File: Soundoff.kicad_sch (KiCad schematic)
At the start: 22 parts, among them J1 Debug, J2 USB-C Receptacle, J4 USB_A, SW1 Pushbutton 4.2x3.2mm 250gf, SW2 Pushbutton 4.2x3.2mm 250gf, U1 3.3V LDO, U16 TLP3123, U4 STM32F042G6Ux

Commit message: v2: make usb-c and pass data through
Signed-off-by: Sean Cross <sean@xobs.io>
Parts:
- removed J4: USB_A, Connector_USB:USB_A_Connfly_DS1095, symbol Connector:USB_A
- removed SW1, SW2: Pushbutton 4.2x3.2mm 250gf, Button_Switch_SMD:SW_Push_1P1T_XKB_TS-1187A, symbol Soundoff:Pushbutton Basic
- added C14, C15, C6: 4.7uF, Capacitor_SMD:C_0402_1005Metric, symbol Soundoff:C 4.7uF 10V 0402
- added C4, C5: 30pF, Capacitor_SMD:C_0603_1608Metric, symbol Device:C_Small
- added P1: Switched USB-C, Soundoff:USB-C-SMD_TYPE-C-31-G-07-1, symbol Soundoff:USB_C_Plug_P24
- added R9: R 5.1k 0402, Resistor_SMD:R_0402_1005Metric, symbol Soundoff:R 5.1k 0402
- added U2: CH334F, Package_DFN_QFN:QFN-24-1EP_4x4mm_P0.5mm_EP2.7x2.7mm, symbol Interface_USB:CH334F
- added U3: EMS4000RSW, Soundoff:QFN-10_1.4x1.8_Pitch0.4mm, symbol Soundoff:EMS4000RSW USB Mux
- added Y1: 12 MHz, 20pF, Crystal:Crystal_SMD_3225-4Pin_3.2x2.5mm, symbol Device:Crystal_GND24_Small
- J1: footprint Connector_PinHeader_2.54mm:PinHeader_1x05_P2.54mm_Vertical -> Connector_PinHeader_2.54mm:PinHeader_1x06_P2.54mm_Vertical; symbol Connector_Generic:Conn_01x05 -> Connector_Generic:Conn_01x06
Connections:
- net BOOT0: now also J1.6 (Pin_6)
- net DBG_USB_D+: now also U2.6 (DP4+); no longer J2.A6 (D+), J2.B6 (D+)
- net DBG_USB_D-: now also U2.5 (DM4-); no longer J2.A7 (D-), J2.B7 (D-)
- net GND: now also C14.2, C15.2, C4.2, C5.2, C6.2, P1.A1 (GND), P1.A12 (GND), P1.B1 (GND), P1.B12 (GND), P1.SH (SHIELD), R9.2, U2.18 (PSELF), U2.25 (GND), U3.3 (GND), U3.8 (EN), Y1.2 (G), Y1.4 (G)
- net VUSB: now also C6.1, U2.19 (V5)
- net 3.0V renamed 3.3V
- net 3.3V: now also C14.1, C15.1, U2.20 (VDD33_{LDO}), U3.9 (VDD)
- net 5V_CONTROL renamed PORT_EN
- net PORT_EN: now also U3.10 (SEL)
- net SWITCHED_5V renamed VUSB_SW
- net VUSB_SW: now also P1.A4 (VBUS), P1.A9 (VBUS), P1.B4 (VBUS), P1.B9 (VBUS)
- new net: P1.A5 (CC), R9.1
- new net: C4.1, U2.4 (XI), Y1.1
- new net: C5.1, U2.3 (XO), Y1.3
- new net TGT_SW_USB_D+: P1.A6 (D+), P1.B6 (D+), U3.7 (L1+)
- new net TGT_SW_USB_D-: P1.A7 (D-), P1.B7 (D-), U3.6 (L1-)
- new net TGT_USB_D+: U2.8 (DP3+), U3.1 (CO+)
- new net TGT_USB_D-: U2.7 (DM3-), U3.2 (CO-)
- new net UFP_USB_D+: J2.A6 (D+), J2.B6 (D+), U2.15 (DPU+)
- new net UFP_USB_D-: J2.A7 (D-), J2.B7 (D-), U2.14 (DMU-)
- no-connect marks 20 -> 42
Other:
- note added: "Switched Port"
- note removed: "Switched Power"
- moved on the sheet: C12, C13

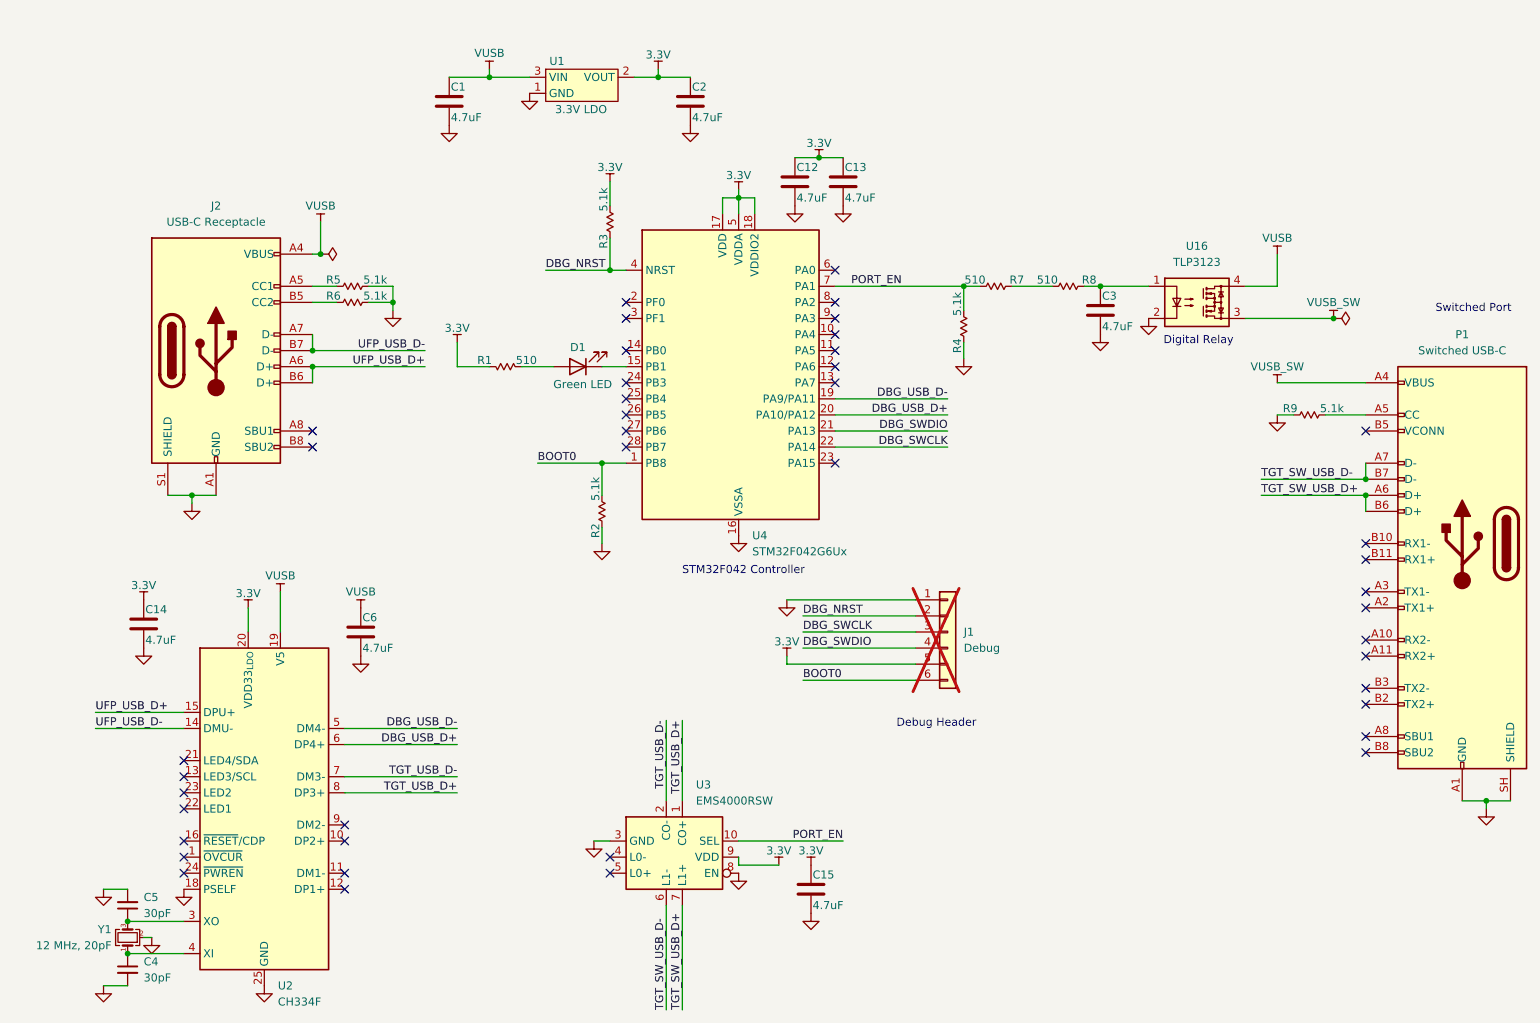
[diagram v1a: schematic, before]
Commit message: v3: fix usb polarity
The USB polarity was incorrect -- the DFP and UFP roles were swapped.
Change the connectors around to make it correct now.

Signed-off-by: Sean Cross <sean@xobs.io>
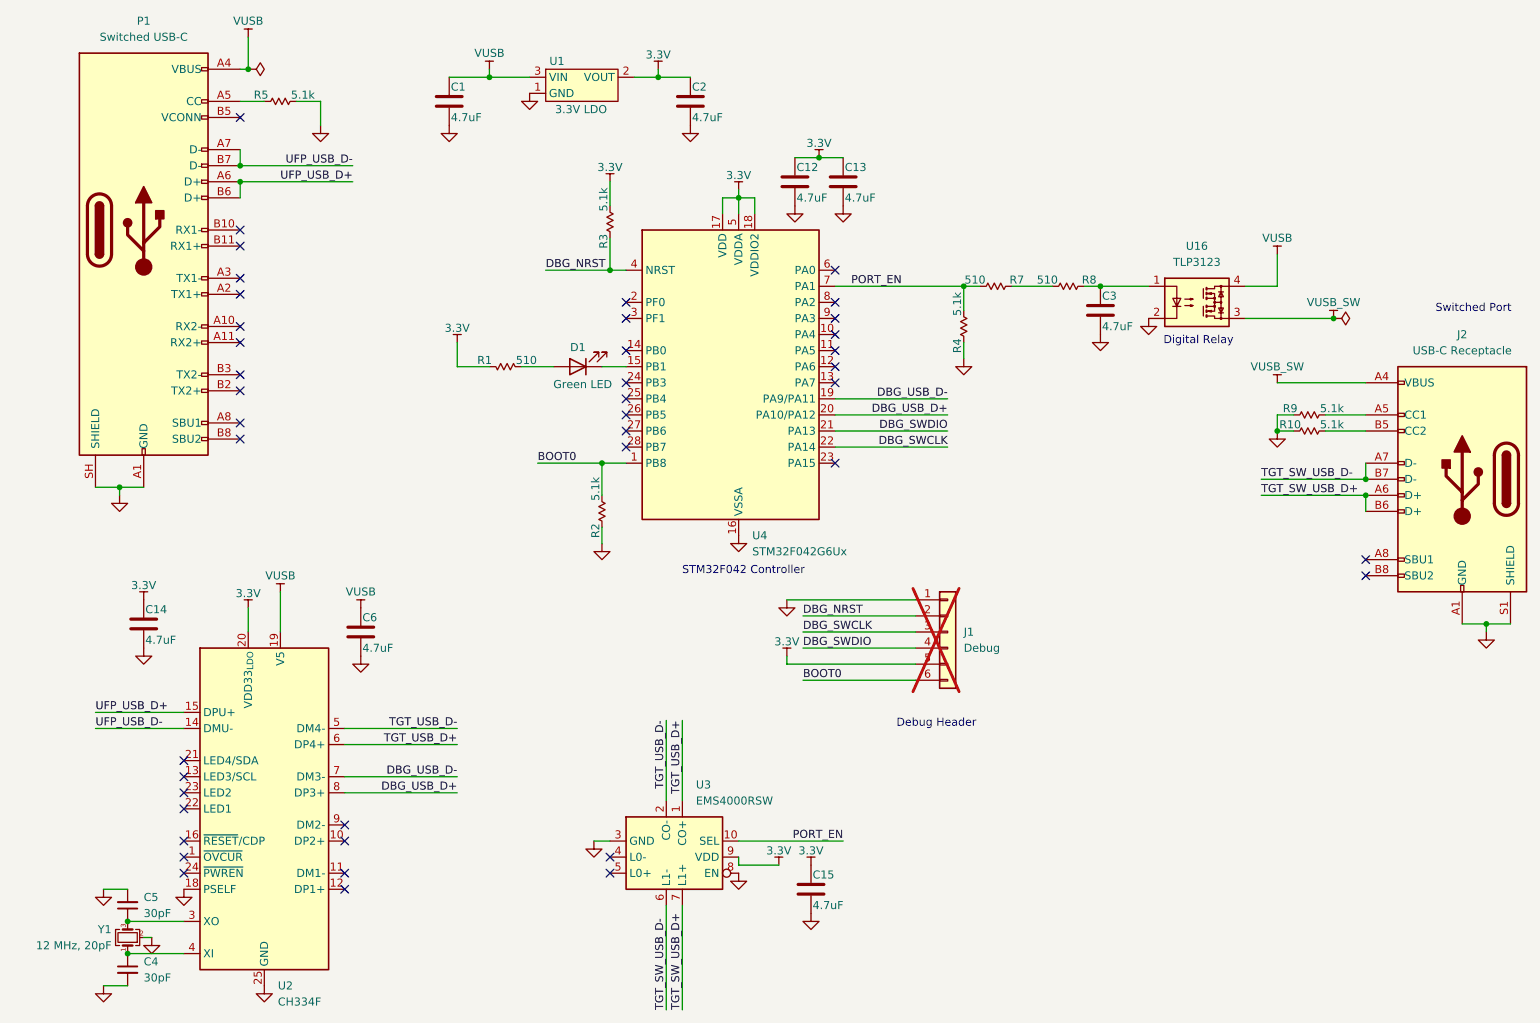
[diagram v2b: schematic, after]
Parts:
- removed R6: R 5.1k 0402, Resistor_SMD:R_0402_1005Metric, symbol Soundoff:R 5.1k 0402
- added R10: R 5.1k 0402, Resistor_SMD:R_0402_1005Metric, symbol Soundoff:R 5.1k 0402
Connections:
- net DBG_USB_D+: now also U2.8 (DP3+); no longer U2.6 (DP4+)
- net DBG_USB_D-: now also U2.7 (DM3-); no longer U2.5 (DM4-)
- net GND: now also R10.2
- net TGT_SW_USB_D+: now also J2.A6 (D+), J2.B6 (D+); no longer P1.A6 (D+), P1.B6 (D+)
- net TGT_SW_USB_D-: now also J2.A7 (D-), J2.B7 (D-); no longer P1.A7 (D-), P1.B7 (D-)
- net TGT_USB_D+: now also U2.6 (DP4+); no longer U2.8 (DP3+)
- net TGT_USB_D-: now also U2.5 (DM4-); no longer U2.7 (DM3-)
- net UFP_USB_D+: now also P1.A6 (D+), P1.B6 (D+); no longer J2.A6 (D+), J2.B6 (D+)
- net UFP_USB_D-: now also P1.A7 (D-), P1.B7 (D-); no longer J2.A7 (D-), J2.B7 (D-)
- net VUSB: now also P1.A4 (VBUS), P1.A9 (VBUS), P1.B4 (VBUS), P1.B9 (VBUS); no longer J2.A4 (VBUS), J2.A9 (VBUS), J2.B4 (VBUS), J2.B9 (VBUS)
- net VUSB_SW: now also J2.A4 (VBUS), J2.A9 (VBUS), J2.B4 (VBUS), J2.B9 (VBUS); no longer P1.A4 (VBUS), P1.A9 (VBUS), P1.B4 (VBUS), P1.B9 (VBUS)
- net at R9.1: now also J2.A5 (CC1); no longer P1.A5 (CC)
- net at R5.2: now also P1.A5 (CC); no longer J2.A5 (CC1)
- net at J2.B5 (CC2): now also R10.1
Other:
- moved on the sheet: J2, P1, R5
